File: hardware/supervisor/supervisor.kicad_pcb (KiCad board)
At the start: 2 copper layers, 149 parts, among them IC1 ULN2003A, IC2 LM2596-3.3, IC3 MAX11612, IC4 ACS723LLCTR-10AU-T, IC5 ACS723LLCTR-10AU-T, IC6 ACS723LLCTR-10AU-T, IC7 NLSX4373, IC8 NLSX4373, IC9 SIM900, K1 RELAY_SERIE_36, K2 RELAY_SERIE_36, P1 CONN_01X02, P2 RASPI-CONNECT, P3 POWER, P4 RELAY CONNECTOR, P5 CONN_01X02, P6 string0, P7 string1, P8 string2, P9 CONN_01X02, SW1 SW_PUSH, SW2 SW_PUSH, U1 SC16IS740IPW, U10 CD74HC4046, U11 CD74HC4046, U12 OPA376AIDCK, U13 CD74HC4046, U14 CD74HC4046, U2 SC16IS740IPW, U3 SC16IS740IPW, U4 RF_CONN, U5 SIM_HOLDER, U6 OPA376AIDCK, U7 CD74HC4046, U8 CD74HC4046, U9 OPA376AIDCK

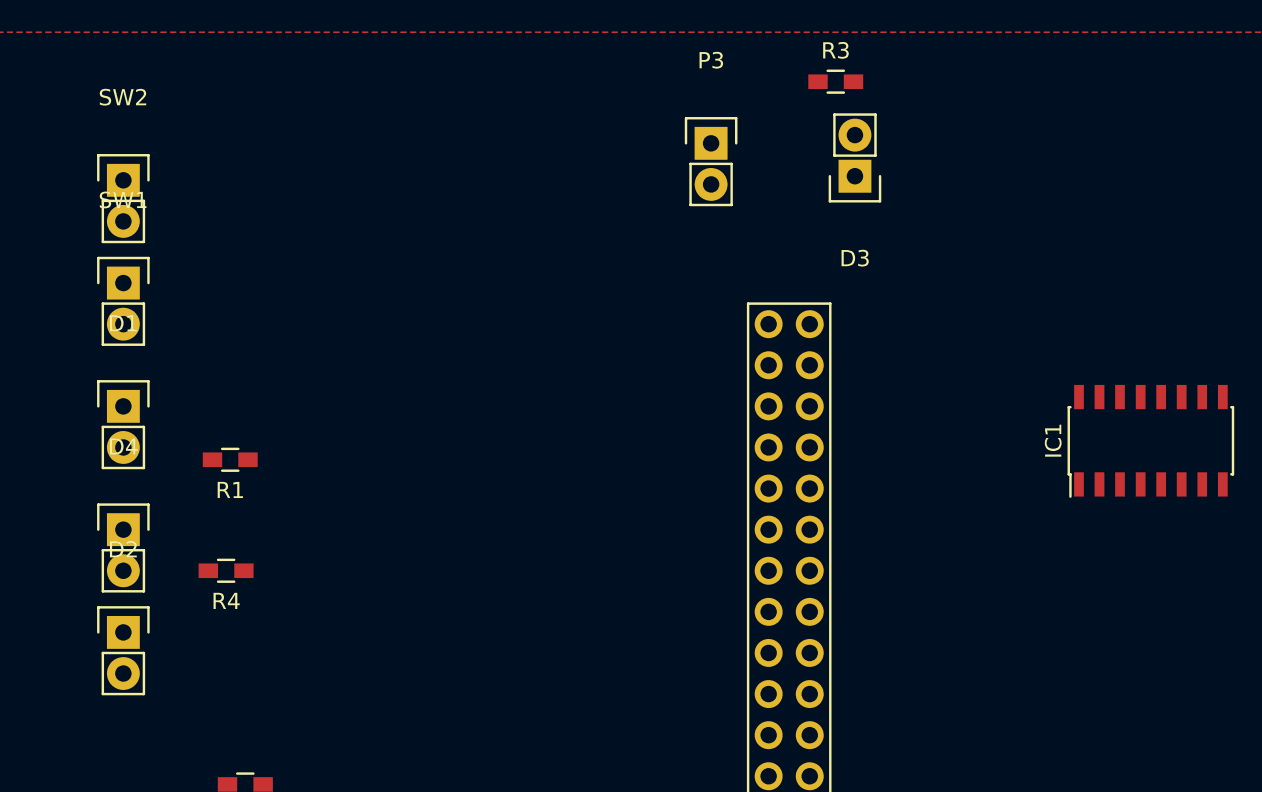
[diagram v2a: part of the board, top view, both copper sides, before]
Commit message: replace 3 leds with SMT
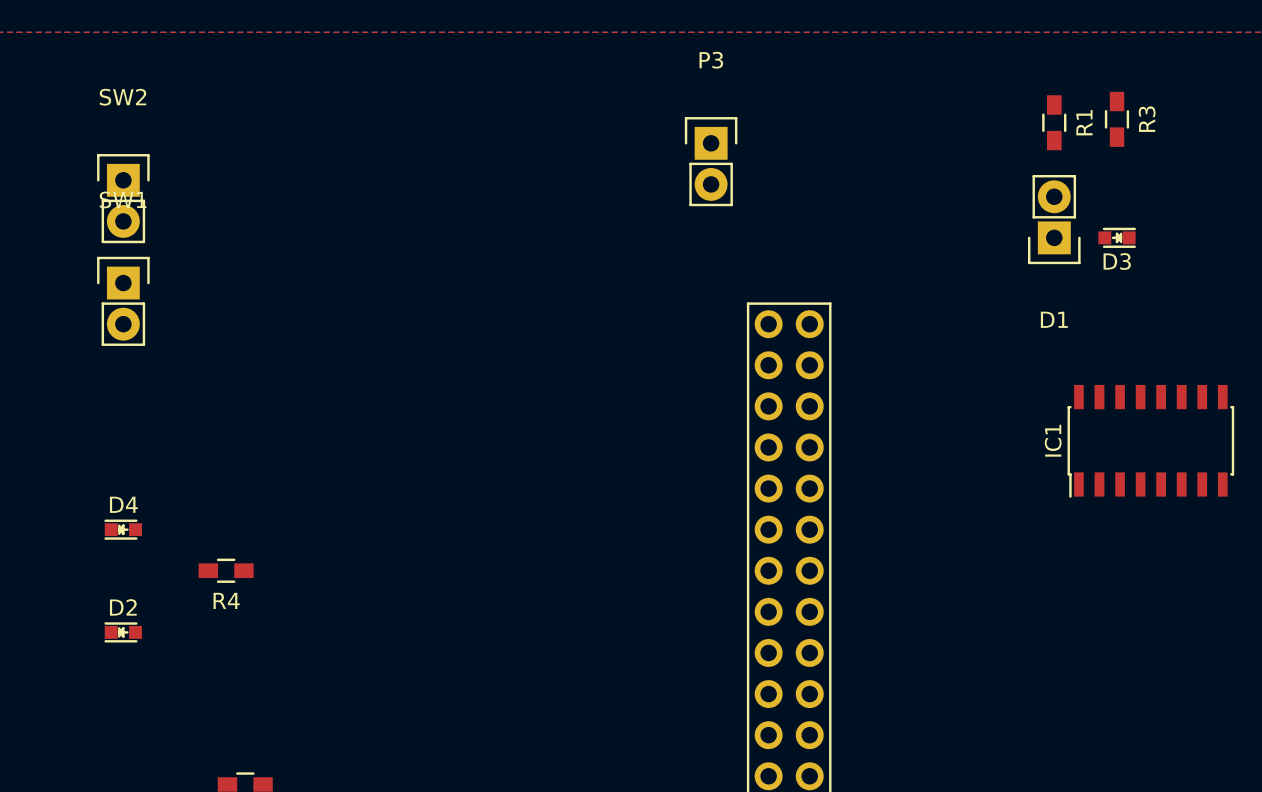
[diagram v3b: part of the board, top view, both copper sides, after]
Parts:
- D2, D3, D4: footprint Pin_Headers:Pin_Header_Straight_1x02 -> LEDs:LED_0603
- moved D1 58.5 mm to (67.7, 12.7), turned to 180 degrees
- moved R1 55.0 mm to (67.7, 5.59), turned to 270 degrees
- moved R3 17.5 mm to (71.6, 5.38), turned to 270 degrees
- moved D3 16.6 mm to (71.6, 12.7)

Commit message: prototype layout for fsk
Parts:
- C6, C7, D5, IC2, IC8, IC9, L1, R5, R6, R7, U4, U5: moved to B.Cu
- moved K2 180.8 mm to (12.2, 76.3), turned to 90 degrees
- moved IC8 179.1 mm to (62.5, 29.9), turned to 90 degrees
- moved R7 174.7 mm to (63.8, 45.0), turned to 90 degrees
- moved IC9 173.3 mm to (88.4, 30.7), turned to 180 degrees
- moved U5 165.8 mm to (85.6, 53.1), turned to 180 degrees
- moved R5 165.3 mm to (66.0, 43.7), turned to 90 degrees
- moved R6 163.8 mm to (70.6, 43.7), turned to 180 degrees
- moved C6 161.5 mm to (62.5, 54.4), turned to 180 degrees
- moved K1 157.6 mm to (34.3, 76.6), turned to 90 degrees
- moved U4 154.9 mm to (96.0, 7.87), turned to 180 degrees
- moved P1 150.9 mm to (53.5, 139.2)
- moved C10 150.9 mm to (59.3, 141.5)
- moved R11 150.9 mm to (55.5, 141.5)
- moved R12 150.9 mm to (59.8, 139.3)
- moved R17 150.9 mm to (60.8, 135.4)
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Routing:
- net /FSK Module 3/coupling3: track 0.00 -> 45.0 mm
- net /FSK Module 3/outgoing3: track 0.00 -> 20.8 mm
- net Net-(R42-Pad2): track 0.00 -> 9.61 mm
- net Net-(C37-Pad2): track 0.00 -> 9.08 mm
- net Net-(C31-Pad1): track 0.00 -> 8.57 mm
- net Net-(C39-Pad2): track 0.00 -> 7.83 mm
- net Net-(R42-Pad1): track 0.00 -> 7.56 mm
- net Net-(R41-Pad1): track 0.00 -> 7.15 mm
- net Net-(C40-Pad2): track 0.00 -> 7.06 mm
- net /FSK Module 3/JP3: track 0.00 -> 6.90 mm
- net Net-(R40-Pad2): track 0.00 -> 6.12 mm
- net Net-(C39-Pad1): track 0.00 -> 5.50 mm
- net Net-(R48-Pad2): track 0.00 -> 5.36 mm
- net Net-(JP3.12-Pad2): track 0.00 -> 5.12 mm
- net Net-(C36-Pad1): track 0.00 -> 5.12 mm
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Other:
- net class 0.4 added: clearance 0.25, trace_width 0.4, via_dia 1, via_drill 0.4
- net class 0.6 added: clearance 0.3, trace_width 0.6, via_dia 1, via_drill 0.4
- net class 0.8 added: clearance 0.3, trace_width 0.8, via_dia 1, via_drill 0.4
- net class 1.0 added: clearance 0.4, trace_width 1, via_dia 1.2, via_drill 0.8

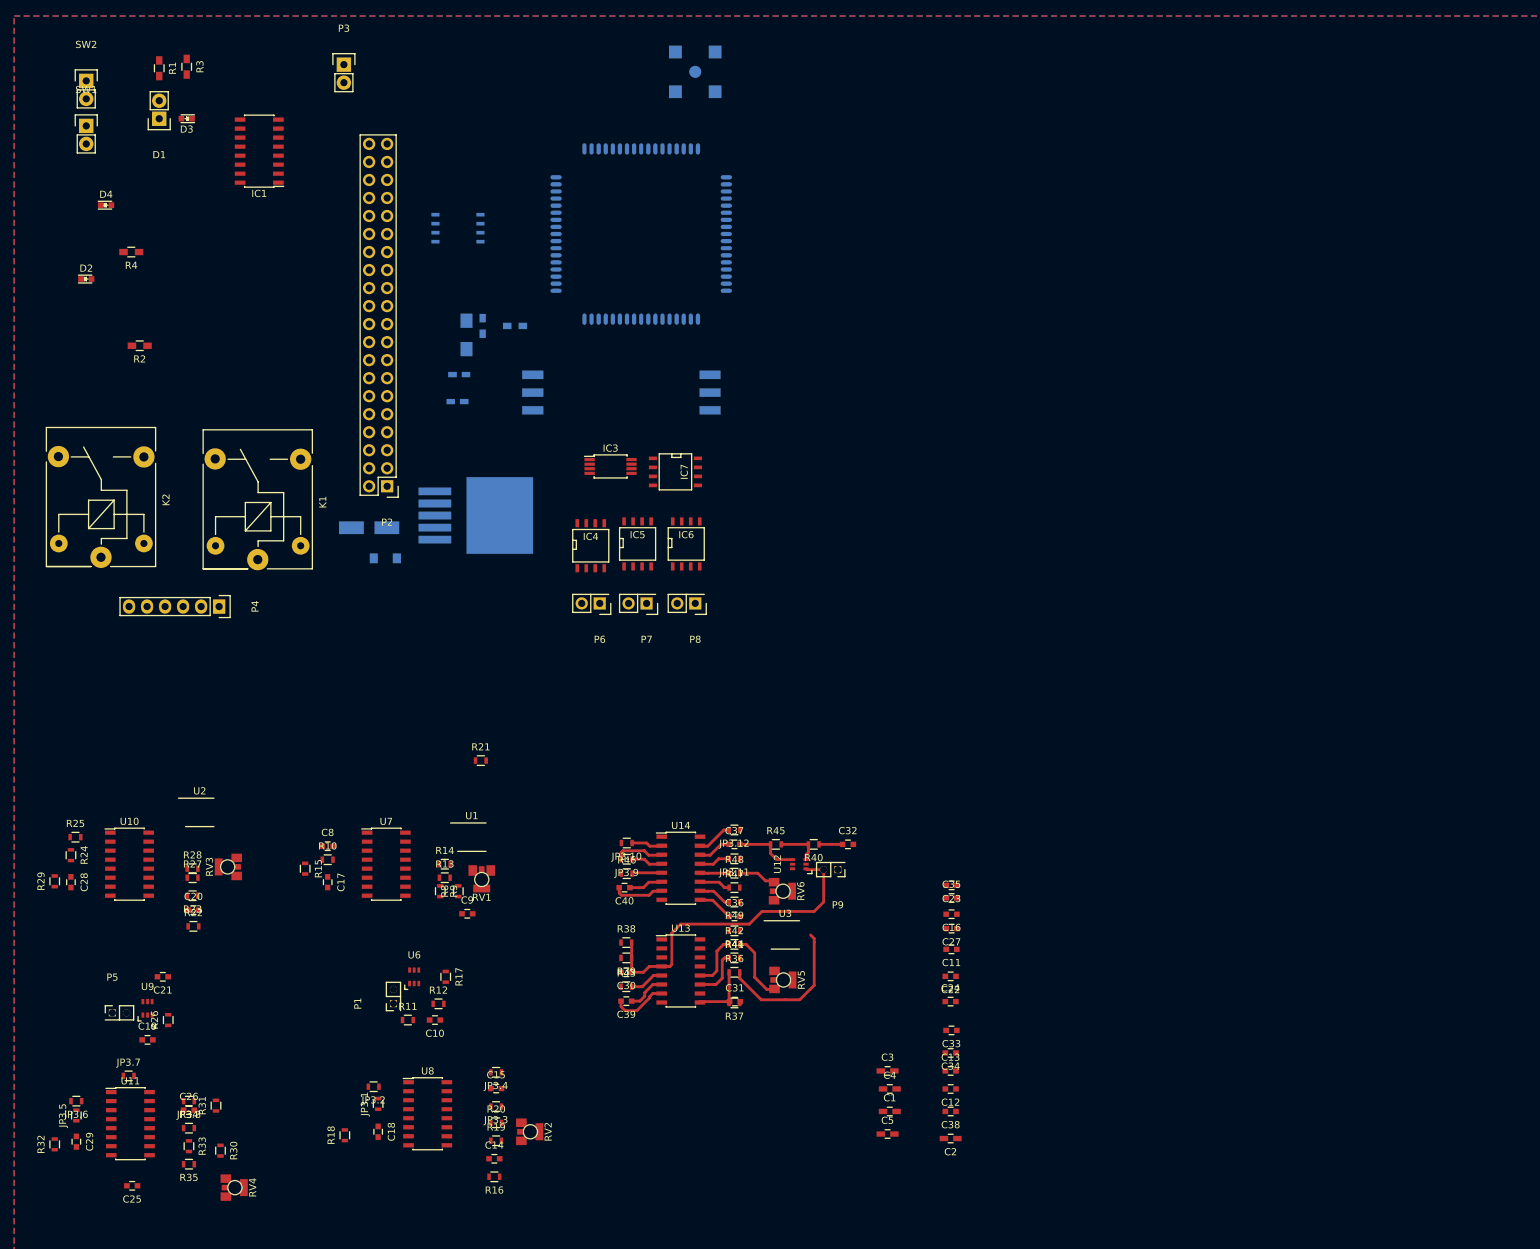
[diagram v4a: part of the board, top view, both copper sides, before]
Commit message: remove unused schematic parts, port changes to master pcb
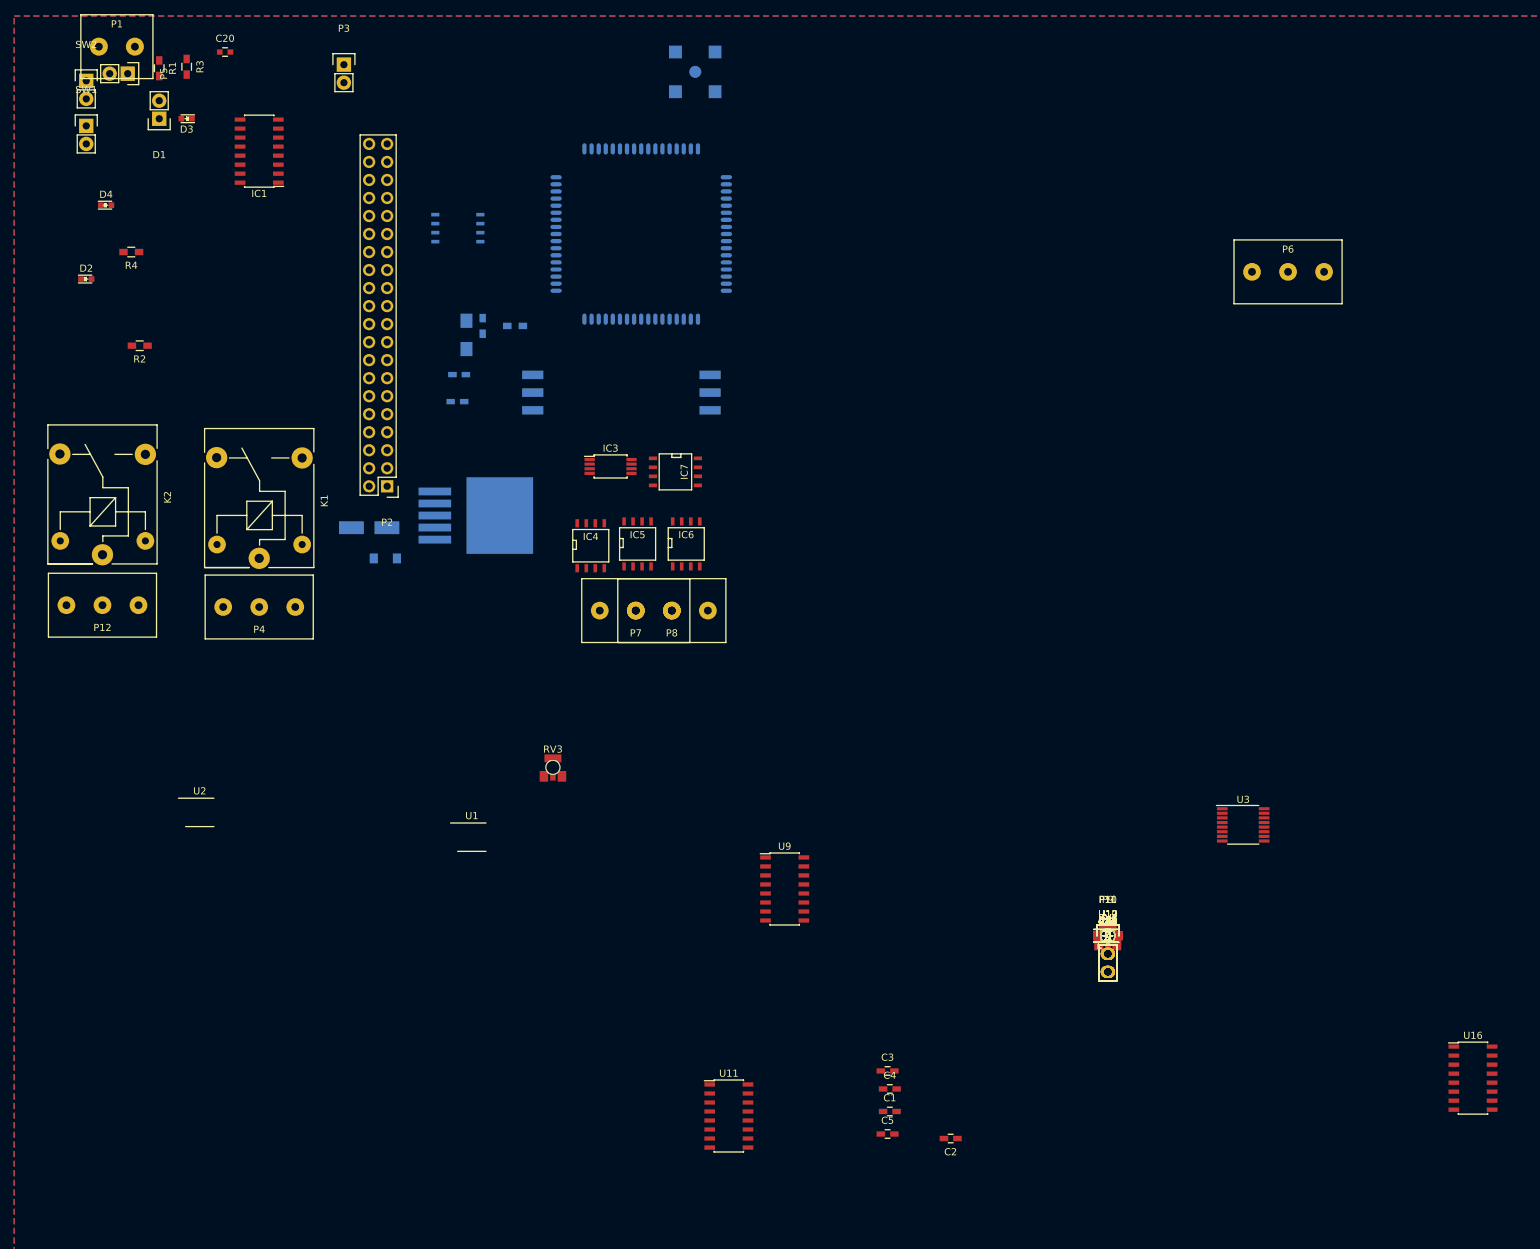
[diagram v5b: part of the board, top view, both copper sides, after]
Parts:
- removed C10, C14, C15, C17, C18, C31, C32, C36, C37, C39, C40, C8, C9: C_Small, Capacitors_SMD:C_0603
- removed C11, C33: 0.1u, Capacitors_SMD:C_0603
- removed C12, C16, C34, C38: 100n, Capacitors_SMD:C_0603
- removed C13, C35: 1u, Capacitors_SMD:C_0603
- removed JP3.1, JP3.10, JP3.11, JP3.12, JP3.2, JP3.3, JP3.4, JP3.5, JP3.6, JP3.7, JP3.8, JP3.9, R12, R13, R14, R16, R17, R19, R20, R40, R41, R42, R44, R45, R47, R48: R_Small, Resistors_SMD:R_0603
- removed R10, R11, R9: 100k, Resistors_SMD:R_0603
- removed R15, R18, R43, R46, R8: 10k, Resistors_SMD:R_0603
- removed R21, R49: 50k, Resistors_SMD:R_0603
- removed RV1, RV2, RV5, RV6: POT, pro4:EVM-1USX30B14_poti
- removed U13, U14, U7, U8: CD74HC4046, Housings_SOIC:SOIC-16_3.9x9.9mm_Pitch1.27mm
- removed U6: OPA376AIDCK, TO_SOT_Packages_SMD:SC-70-6
- added C42: C_Small, Capacitors_SMD:C_0805, F.Cu at (154.2, 129.7)
- added C43, C46, C47: C_Small, Capacitors_SMD:C_0603, F.Cu at (154.2, 129.7)
- added C44: 100n, Capacitors_SMD:C_0603, F.Cu at (154.2, 129.7)
- added C45: 0.1u, Capacitors_SMD:C_0603, F.Cu at (154.2, 129.7)
- added D6, D7, D8: D_Schottky_Small, Diodes_SMD:SOD-123, F.Cu at (154.2, 129.7)
- added P10, P11: CONN_01X03, Pin_Headers:Pin_Header_Straight_1x03, F.Cu at (154.2, 129.7)
- added P12: CONN_01X03, pro4:CONNECTOR-relay, F.Cu at (12.4, 83.1)
- added R54: 10k, Resistors_SMD:R_0603, F.Cu at (154.2, 129.7)
- added R55: x, Resistors_SMD:R_0603, F.Cu at (154.2, 129.7)
- added R56, R60, R61: 100k, Resistors_SMD:R_0603, F.Cu at (154.2, 129.7)
- added R57, R58, R59, R62: R_Small, Resistors_SMD:R_0603, F.Cu at (154.2, 129.7)
- added RV7: POT, pro4:EVM-1USX30B14_poti, F.Cu at (154.2, 129.7)
- added U16: CD74HC4046, Housings_SOIC:SOIC-16_3.9x9.9mm_Pitch1.27mm, F.Cu at (205.6, 149.7)
- added U17: OPA376AIDCK, TO_SOT_Packages_SMD:SC-70-6, F.Cu at (154.2, 129.7)
- C19, C25: footprint Capacitors_SMD:C_0603 -> Capacitors_SMD:C_0805
- C21: value C_Small -> 100n
- C23: value 100n -> C_Small
- C24: value 1u -> C_Small
- C28: value C_Small -> 0.1u
- P1: value CONN_01X02 -> 230V_IN; footprint Pin_Headers:Pin_Header_Straight_2x01 -> pro4:CONNECTOR-input
- P4: value RELAY CONNECTOR -> CONN_01X03; footprint Pin_Headers:Pin_Header_Straight_1x06 -> pro4:CONNECTOR-relay
- P5: value CONN_01X02 -> 230V_OUT; footprint Pin_Headers:Pin_Header_Straight_2x01 -> Pin_Headers:Pin_Header_Straight_1x02
- P6: value string0 -> CONN_01X03; footprint Pin_Headers:Pin_Header_Straight_2x01 -> pro4:CONNECTOR-relay
- P7: value string1 -> CONN_01X03; footprint Pin_Headers:Pin_Header_Straight_2x01 -> pro4:CONNECTOR-relay
- P8: value string2 -> CONN_01X03; footprint Pin_Headers:Pin_Header_Straight_2x01 -> pro4:CONNECTOR-relay
- P9: value CONN_01X02 -> CONN_01X03; footprint Pin_Headers:Pin_Header_Straight_2x01 -> Pin_Headers:Pin_Header_Straight_1x03
- R23: value 100k -> x
- R25, R39: value 100k -> R_Small
- R28, R33: value R_Small -> 100k
- R29: value 10k -> 100k
- R31: value R_Small -> 10k
- R32: value 10k -> x
- R35: value 50k -> R_Small
- R36: value 10k -> R_Small
- U10: value CD74HC4046 -> OPA376AIDCK; footprint Housings_SOIC:SOIC-16_3.9x9.9mm_Pitch1.27mm -> TO_SOT_Packages_SMD:SC-70-6
- U9: value OPA376AIDCK -> CD74HC4046; footprint TO_SOT_Packages_SMD:SC-70-6 -> Housings_SOIC:SOIC-16_3.9x9.9mm_Pitch1.27mm
- moved R32 151.3 mm to (154.2, 129.7), turned to 0 degrees
- moved R29 148.7 mm to (154.2, 129.7), turned to 0 degrees
- moved C29 148.3 mm to (154.2, 129.7), turned to 0 degrees
- moved R24 146.6 mm to (154.2, 129.7), turned to 0 degrees
- moved C28 146.4 mm to (154.2, 129.7), turned to 0 degrees
- moved R25 146.2 mm to (154.2, 129.7)
- moved C25 142.0 mm to (154.2, 129.7), turned to 0 degrees
- moved P1 140.4 mm to (14.5, 4.32), turned to 0 degrees
- moved U10 138.3 mm to (154.2, 129.7)
- moved C19 136.2 mm to (154.2, 129.7)
- moved R35 133.5 mm to (154.2, 129.7), turned to 0 degrees
- moved C21 133.3 mm to (154.2, 129.7), turned to 0 degrees
- moved R26 133.0 mm to (154.2, 129.7), turned to 0 degrees
- moved R33 132.9 mm to (154.2, 129.7), turned to 0 degrees
- moved P5 132.4 mm to (16.0, 8.13), turned to 270 degrees
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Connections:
- C19 pad 1: /FSK Module 2/coupling2 -> Net-(C19-Pad1)
- C19 pad 2: GND -> /FSK Module 1/coupling1
- C21 pad 1: Net-(C21-Pad1) -> +3V3
- C22 pad 1: +3V3 -> Net-(C22-Pad1)
- C23 pad 1: +3V3 -> Net-(C23-Pad1)
- C23 pad 2: GND -> Net-(C23-Pad2)
- C24 pad 1: GND -> /FSK Module 1/incoming1
- C24 pad 2: +3V3 -> GND
- C25 pad 2: GND -> /FSK Module 2/coupling2
- C26 pad 2: Net-(C26-Pad2) -> GND
- C28 pad 2: Net-(C28-Pad2) -> GND
- C30 pad 1: /FSK Module 3/coupling3 -> /FSK Module 2/incoming2
- P1 pad 1: GND -> Net-(P1-Pad1)
- P1 pad 2: /FSK Module 1/coupling1 -> Net-(P1-Pad2)
- P2 pad 1: +3V3 -> (no net)
- P2 pad 17: +3V3 -> (no net)
- P2 pad 22: (no net) -> ENSK0
- P2 pad 26: (no net) -> ENSK1
- P2 pad 32: (no net) -> ENSK2
- P5 pad 1: GND -> Net-(P1-Pad2)
- P5 pad 2: /FSK Module 2/coupling2 -> Net-(P1-Pad1)
- P6 pad 2: string_in0 -> PGND0
- P7 pad 2: string_in1 -> PGND1
- P8 pad 2: string_in2 -> PGND2
- P9 pad 1: GND -> PGND2
- P9 pad 2: /FSK Module 3/coupling3 -> Net-(C19-Pad1)
- R22 pad 2: /FSK Module 2/outgoing2 -> /FSK Module 1/outgoing1
- R23 pad 1: +3V3 -> Net-(C20-Pad1)
- R23 pad 2: Net-(C20-Pad1) -> GND
- R24 pad 2: /FSK Module 2/coupling2 -> Net-(C20-Pad1)
- R25 pad 1: /FSK Module 2/coupling2 -> Net-(R25-Pad1)
- R26 pad 1: Net-(C21-Pad1) -> Net-(R26-Pad1)
- R27 pad 1: Net-(R27-Pad1) -> GND
- R27 pad 2: GND -> Net-(C22-Pad1)
- R29 pad 1: GND -> Net-(R28-Pad2)
- R29 pad 2: Net-(R29-Pad2) -> GND
- R30 pad 1: /FSK Module 2/VCOin2 -> /FSK Module 1/incoming1
- R30 pad 2: Net-(C25-Pad1) -> Net-(R28-Pad1)
- R31 pad 1: Net-(C26-Pad2) -> Net-(C26-Pad1)
- R31 pad 2: Net-(R26-Pad2) -> /FSK Module 2/outgoing2
- R32 pad 1: GND -> Net-(C26-Pad1)
- R32 pad 2: Net-(R32-Pad2) -> GND
- R33 pad 1: Net-(R33-Pad1) -> +3V3
- R33 pad 2: GND -> Net-(C26-Pad1)
- R34 pad 2: Net-(R34-Pad2) -> GND
- R35 pad 1: GND -> Net-(R35-Pad1)
- R35 pad 2: /FSK Module 2/incoming2 -> Net-(R35-Pad2)
- R36 pad 1: Net-(C31-Pad1) -> GND
- R36 pad 2: /FSK Module 3/outgoing3 -> Net-(C28-Pad1)
- R37 pad 1: +3V3 -> Net-(R37-Pad1)
- R37 pad 2: Net-(C31-Pad1) -> Net-(R37-Pad2)
- R38 pad 1: +3V3 -> Net-(R37-Pad2)
- R38 pad 2: /FSK Module 3/coupling3 -> GND
- R39 pad 1: /FSK Module 3/coupling3 -> /FSK Module 2/incoming2
- R39 pad 2: GND -> Net-(R37-Pad1)
- RV3 pad 3: Net-(R28-Pad2) -> Net-(R26-Pad2)
- RV4 pad 1: Net-(R34-Pad2) -> (no net)
- RV4 pad 3: (no net) -> Net-(R35-Pad2)
- U10 pad 1: (no net) -> Net-(C22-Pad1)
- U10 pad 2: (no net) -> GND
- U10 pad 3: GND -> Net-(R28-Pad2)
- U10 pad 4: /FSK Module 2/coupling2 -> Net-(R28-Pad1)
- U10 pad 5: Net-(R29-Pad2) -> +3V3
- U10 pad 6: Net-(C28-Pad1) -> (no net)
- U11 pad 10: /FSK Module 2/incoming2 -> (no net)
- U11 pad 11: Net-(R33-Pad1) -> Net-(R34-Pad1)
- U11 pad 12: Net-(R34-Pad1) -> Net-(R35-Pad1)
- U11 pad 13: Net-(JP3.7-Pad2) -> (no net)
- U11 pad 14: Net-(C26-Pad1) -> GND
- U11 pad 15: Net-(JP3.8-Pad2) -> (no net)
- U11 pad 2: Net-(JP3.6-Pad1) -> (no net)
- U11 pad 3: /FSK Module 2/JP2 -> GND
- U11 pad 4: Net-(JP3.5-Pad1) -> /FSK Module 2/coupling2
- U11 pad 5: Net-(R32-Pad2) -> ENSK1
- U11 pad 9: Net-(C25-Pad1) -> Net-(C26-Pad1)
- U12 pad 1: /FSK Module 3/coupling3 -> Net-(C28-Pad1)
- U12 pad 3: Net-(R40-Pad2) -> Net-(R37-Pad2)
- U12 pad 4: Net-(C37-Pad2) -> Net-(R37-Pad1)
- U9 pad 1: /FSK Module 2/coupling2 -> (no net)
- U9 pad 2: GND -> (no net)
- U9 pad 3: Net-(R26-Pad2) -> GND
- U9 pad 4: Net-(C26-Pad2) -> /FSK Module 1/coupling1
- U9 pad 5: +3V3 -> ENSK2
- U9 pad 6: (no net) -> Net-(C23-Pad1)
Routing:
- net /FSK Module 3/coupling3: track 45.0 -> 0.00 mm
- net /FSK Module 3/outgoing3: track 20.8 -> 0.00 mm
- net Net-(R42-Pad2): track 9.61 -> 0.00 mm
- net Net-(C37-Pad2): track 9.08 -> 0.00 mm
- net Net-(C31-Pad1): track 8.57 -> 0.00 mm
- net Net-(C39-Pad2): track 7.83 -> 0.00 mm
- net Net-(R42-Pad1): track 7.56 -> 0.00 mm
- net Net-(R41-Pad1): track 7.15 -> 0.00 mm
- net Net-(C40-Pad2): track 7.06 -> 0.00 mm
- net /FSK Module 3/JP3: track 6.90 -> 0.00 mm
- net Net-(R40-Pad2): track 6.12 -> 0.00 mm
- net Net-(C39-Pad1): track 5.50 -> 0.00 mm
- net Net-(R48-Pad2): track 5.36 -> 0.00 mm
- net Net-(JP3.12-Pad2): track 5.12 -> 0.00 mm
- net Net-(C36-Pad1): track 5.12 -> 0.00 mm
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
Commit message: master grouping done
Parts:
- added P13: 230V_OUT, Pin_Headers:Pin_Header_Straight_1x02, F.Cu at (54.1, 78.0)
- added P14: 230V_OUT, Pin_Headers:Pin_Header_Straight_1x02, F.Cu at (69.6, 78.5)
- added P15: 230V_OUT, Pin_Headers:Pin_Header_Straight_1x02, F.Cu at (86.9, 79.0)
- C1: footprint Capacitors_SMD:C_0603_HandSoldering -> Capacitors_ThroughHole:C_Radial_D7.5_L11.2_P2.5
- C19, C25, C42: footprint Capacitors_SMD:C_0805 -> Pin_Headers:Pin_Header_Straight_1x02
- C2: value C_Small -> CP_Small; footprint Capacitors_SMD:C_0603_HandSoldering -> Capacitors_ThroughHole:C_Radial_D7.5_L11.2_P2.5
- D5: footprint Diodes_SMD:SMA_Handsoldering -> Diodes_SMD:SMB-SMC_Universal_Handsoldering
- L1: footprint Inductors_NEOSID:Neosid_Inductor_SM1206 -> pro4:HC9-large
- moved C20 201.4 mm to (130.3, 179.6)
- moved C5 159.2 mm to (279.1, 189.5)
- moved C3 159.2 mm to (279.1, 180.6)
- moved C4 159.2 mm to (279.5, 183.1)
- moved C29 156.2 mm to (5.59, 177.9)
- moved D7 155.2 mm to (5.70, 174.8)
- moved R32 149.5 mm to (14.9, 183.8), turned to 180 degrees
- moved R34 140.1 mm to (22.6, 177.9)
- moved R35 139.5 mm to (22.6, 176.1)
- moved C27 137.8 mm to (273.8, 198.1)
- moved U16 136.9 mm to (71.6, 177.6)
- moved C21 136.6 mm to (273.8, 195.6)
- moved RV4 135.5 mm to (27.3, 177.2), turned to 90 degrees
- moved C30 133.7 mm to (22.8, 154.5), turned to 270 degrees
- moved R31 133.3 mm to (22.7, 151.6), turned to 180 degrees
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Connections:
- P6 pad 3: string_in0 -> Net-(P13-Pad1)
- P7 pad 3: string_in1 -> Net-(P14-Pad1)
- P8 pad 3: string_in2 -> Net-(P15-Pad1)
